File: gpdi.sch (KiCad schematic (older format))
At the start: 20 parts, among them U1 LFE5U-85F-6BG381C, U11 PCA9306D

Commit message: schematics: Additional field "Koncar" with their specific part number aliases
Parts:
- GPDI1: Koncar (none) -> FX001
- R24: Koncar (none) -> FR003
- U11: Koncar (none) -> FU008
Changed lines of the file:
@@
 F 12 "609-4614-1-ND" H 8950 2950 50  0001 C CNN "Digikey"
 F 13 "A136174CT-ND" H 8950 2950 50  0001 C CNN "Digikey2"
+F 14 "FX001" H 8950 2950 50  0001 C CNN "Koncar"
 	1    8950 2950
 	1    0    0    -1
@@
 F 8 "P100KHCT-ND" V 6100 4700 50  0001 C CNN "Digikey"
 F 9 "Leave empty" V 6100 4700 50  0001 C CNN "LowCost"
+F 10 "FR003" V 6100 4700 50  0001 C CNN "Koncar"
 	1    6100 4700
 	1    0    0    -1
@@
 F 8 "568-4215-1-ND" H 5550 5550 50  0001 C CNN "Digikey"
 F 9 "Leave empty" H 5550 5550 50  0001 C CNN "LowCost"
+F 10 "FU008" H 5550 5550 50  0001 C CNN "Koncar"
 	1    5550 5550
 	1    0    0    -1

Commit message: schematics: add "Side" field for parts which appear on top side
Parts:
- GPDI1: Side (none) -> T
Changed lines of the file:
@@
 F 13 "A136174CT-ND" H 8950 2950 50  0001 C CNN "Digikey2"
 F 14 "FX001" H 8950 2950 50  0001 C CNN "Koncar"
+F 15 "T" H 8950 2950 50  0001 C CNN "Side"
 	1    8950 2950
 	1    0    0    -1

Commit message: schematics: updating LowCost fields
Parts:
- R24, R25, R26: LowCost Leave empty -> (none)
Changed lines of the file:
@@
 Title "ULX3S"
 Date ""
-Rev "1.0.1"
+Rev "1.0.2"
 Comp "EMARD"
 Comment1 "General Purpose Differential Interface"
@@
 F 7 "71-CRCW0603100KFKEAC" V 6100 4700 50  0001 C CNN "Mouser2"
 F 8 "P100KHCT-ND" V 6100 4700 50  0001 C CNN "Digikey"
-F 9 "Leave empty" V 6100 4700 50  0001 C CNN "LowCost"
-F 10 "FR003" V 6100 4700 50  0001 C CNN "Koncar"
+F 9 "FR003" V 6100 4700 50  0001 C CNN "Koncar"
 	1    6100 4700
 	1    0    0    -1
@@
 F 2 "Resistor_SMD:R_0603_1608Metric" V 6230 4700 50  0001 C CNN
 F 3 "" H 6300 4700 50  0000 C CNN
-F 4 "Leave empty" V 6300 4700 50  0001 C CNN "LowCost"
 	1    6300 4700
 	1    0    0    -1
@@
 F 2 "Resistor_SMD:R_0603_1608Metric" V 6430 4700 50  0001 C CNN
 F 3 "" H 6500 4700 50  0000 C CNN
-F 4 "Leave empty" V 6500 4700 50  0001 C CNN "LowCost"
 	1    6500 4700
 	1    0    0    -1

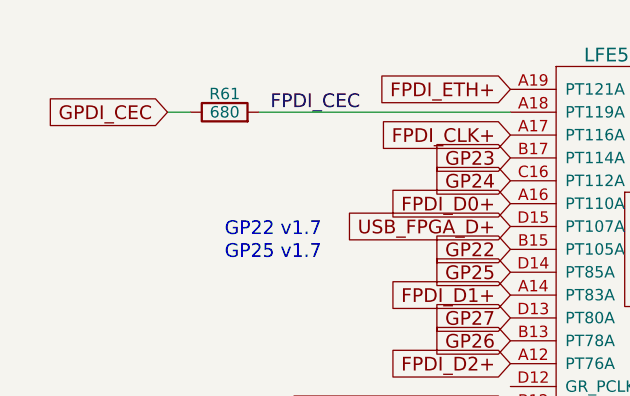
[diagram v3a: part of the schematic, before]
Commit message: schematics: change resistor value 680->590 ohm to improve DAC
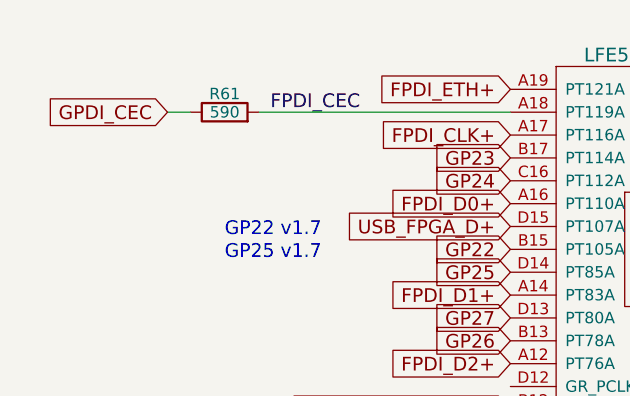
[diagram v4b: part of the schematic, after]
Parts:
- R61: value 680 -> 590
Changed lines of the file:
@@
 P 1600 2300
 F 0 "R61" V 1680 2300 50  0000 C CNN
-F 1 "680" V 1600 2300 50  0000 C CNN
+F 1 "590" V 1600 2300 50  0000 C CNN
 F 2 "Resistor_SMD:R_0603_1608Metric" V 1530 2300 50  0001 C CNN
 F 3 "" H 1600 2300 50  0000 C CNN

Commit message: schematics: DAC closer to 75 ohm impedance: 130, 270, 550 ohm
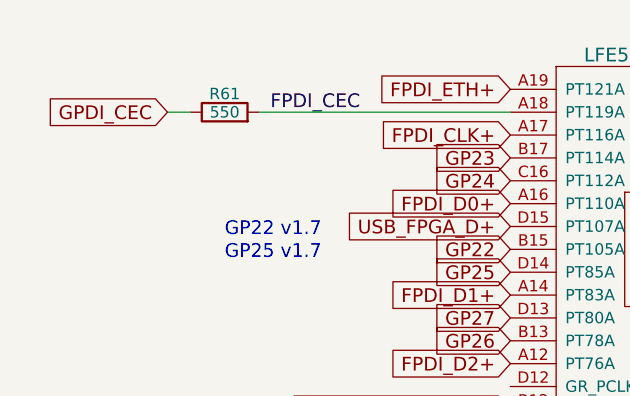
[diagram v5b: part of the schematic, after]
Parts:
- R61: value 590 -> 550
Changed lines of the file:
@@
 P 1600 2300
 F 0 "R61" V 1680 2300 50  0000 C CNN
-F 1 "590" V 1600 2300 50  0000 C CNN
+F 1 "550" V 1600 2300 50  0000 C CNN
 F 2 "Resistor_SMD:R_0603_1608Metric" V 1530 2300 50  0001 C CNN
 F 3 "" H 1600 2300 50  0000 C CNN

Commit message: schematics: updating DAC 550->549 ohm, 1.2k->1.1k
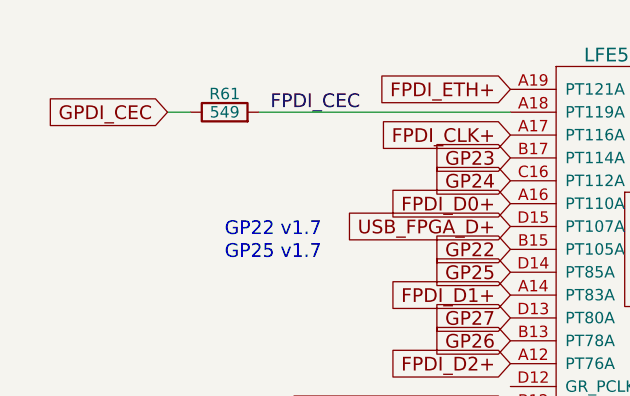
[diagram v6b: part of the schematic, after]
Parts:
- R61: value 550 -> 549
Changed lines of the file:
@@
 P 1600 2300
 F 0 "R61" V 1680 2300 50  0000 C CNN
-F 1 "550" V 1600 2300 50  0000 C CNN
+F 1 "549" V 1600 2300 50  0000 C CNN
 F 2 "Resistor_SMD:R_0603_1608Metric" V 1530 2300 50  0001 C CNN
 F 3 "" H 1600 2300 50  0000 C CNN

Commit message: schematics: cheaper manufacturers PNs and some prices
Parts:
- GPDI1: Mouser_price100 (none) -> 0.439€; Onlinecomponents (none) -> 10029449-111RLF; Onlinecomponents_price100 (none) -> 0.364$
- U11: Newark (none) -> 70R6428; Newark_price100 (none) -> 0.212$
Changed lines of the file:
@@
 F 9 "www.mouser.com" H 8950 2950 60  0001 C CNN "Mouser_URL"
 F 10 "649-10029449-111RLF" H 8950 2950 60  0001 C CNN "Mouser"
-F 11 "571-5-1903015-5" H 8950 2950 50  0001 C CNN "Mouser2"
-F 12 "609-4614-1-ND" H 8950 2950 50  0001 C CNN "Digikey"
-F 13 "A136174CT-ND" H 8950 2950 50  0001 C CNN "Digikey2"
-F 14 "FX001" H 8950 2950 50  0001 C CNN "Koncar"
-F 15 "T" H 8950 2950 50  0001 C CNN "Side"
+F 11 "0.439€" H 8950 2950 50  0001 C CNN "Mouser_price100"
+F 12 "571-5-1903015-5" H 8950 2950 50  0001 C CNN "Mouser2"
+F 13 "609-4614-1-ND" H 8950 2950 50  0001 C CNN "Digikey"
+F 14 "A136174CT-ND" H 8950 2950 50  0001 C CNN "Digikey2"
+F 15 "10029449-111RLF" H 8950 2950 50  0001 C CNN "Onlinecomponents"
+F 16 "0.364$" H 8950 2950 50  0001 C CNN "Onlinecomponents_price100"
+F 17 "FX001" H 8950 2950 50  0001 C CNN "Koncar"
+F 18 "T" H 8950 2950 50  0001 C CNN "Side"
 	1    8950 2950
 	1    0    0    -1
@@
 F 7 "771-PCA9306D-T" H 5550 5550 50  0001 C CNN "Mouser"
 F 8 "568-4215-1-ND" H 5550 5550 50  0001 C CNN "Digikey"
-F 9 "Leave empty" H 5550 5550 50  0001 C CNN "LowCost"
-F 10 "FU008" H 5550 5550 50  0001 C CNN "Koncar"
+F 9 "70R6428" H 5550 5550 50  0001 C CNN "Newark"
+F 10 "0.212$" H 5550 5550 50  0001 C CNN "Newark_price100"
+F 11 "Leave empty" H 5550 5550 50  0001 C CNN "LowCost"
+F 12 "FU008" H 5550 5550 50  0001 C CNN "Koncar"
 	1    5550 5550
 	1    0    0    -1

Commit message: renaming *_price -> price_* fields that may be misinterpreted by 1-clock-bom
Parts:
- GPDI1: Mouser_price100 0.439€ -> (none); Onlinecomponents_price100 0.364$ -> (none); price100_Mouser (none) -> 0.439€; price100_Onlinecomponents (none) -> 0.364$
- U11: Newark_price100 0.212$ -> (none); price100_Newark (none) -> 0.212$
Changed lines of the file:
@@
 F 9 "www.mouser.com" H 8950 2950 60  0001 C CNN "Mouser_URL"
 F 10 "649-10029449-111RLF" H 8950 2950 60  0001 C CNN "Mouser"
-F 11 "0.439€" H 8950 2950 50  0001 C CNN "Mouser_price100"
+F 11 "0.439€" H 8950 2950 50  0001 C CNN "price100_Mouser"
 F 12 "571-5-1903015-5" H 8950 2950 50  0001 C CNN "Mouser2"
 F 13 "609-4614-1-ND" H 8950 2950 50  0001 C CNN "Digikey"
 F 14 "A136174CT-ND" H 8950 2950 50  0001 C CNN "Digikey2"
 F 15 "10029449-111RLF" H 8950 2950 50  0001 C CNN "Onlinecomponents"
-F 16 "0.364$" H 8950 2950 50  0001 C CNN "Onlinecomponents_price100"
+F 16 "0.364$" H 8950 2950 50  0001 C CNN "price100_Onlinecomponents"
 F 17 "FX001" H 8950 2950 50  0001 C CNN "Koncar"
 F 18 "T" H 8950 2950 50  0001 C CNN "Side"
@@
 F 8 "568-4215-1-ND" H 5550 5550 50  0001 C CNN "Digikey"
 F 9 "70R6428" H 5550 5550 50  0001 C CNN "Newark"
-F 10 "0.212$" H 5550 5550 50  0001 C CNN "Newark_price100"
+F 10 "0.212$" H 5550 5550 50  0001 C CNN "price100_Newark"
 F 11 "Leave empty" H 5550 5550 50  0001 C CNN "LowCost"
 F 12 "FU008" H 5550 5550 50  0001 C CNN "Koncar"
